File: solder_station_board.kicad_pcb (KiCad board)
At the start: 2 copper layers, 104.6 x 55.9 mm, 44 parts, among them J1 PWR_5_36, J2 Conn_FB, J3 RT_WELLER, J4 VFD dISPLAY, J5 INPUT, J6 PWR_15V, J7 INT_PWR, J8 SERIAL, J9 INPUT, P1 ISP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

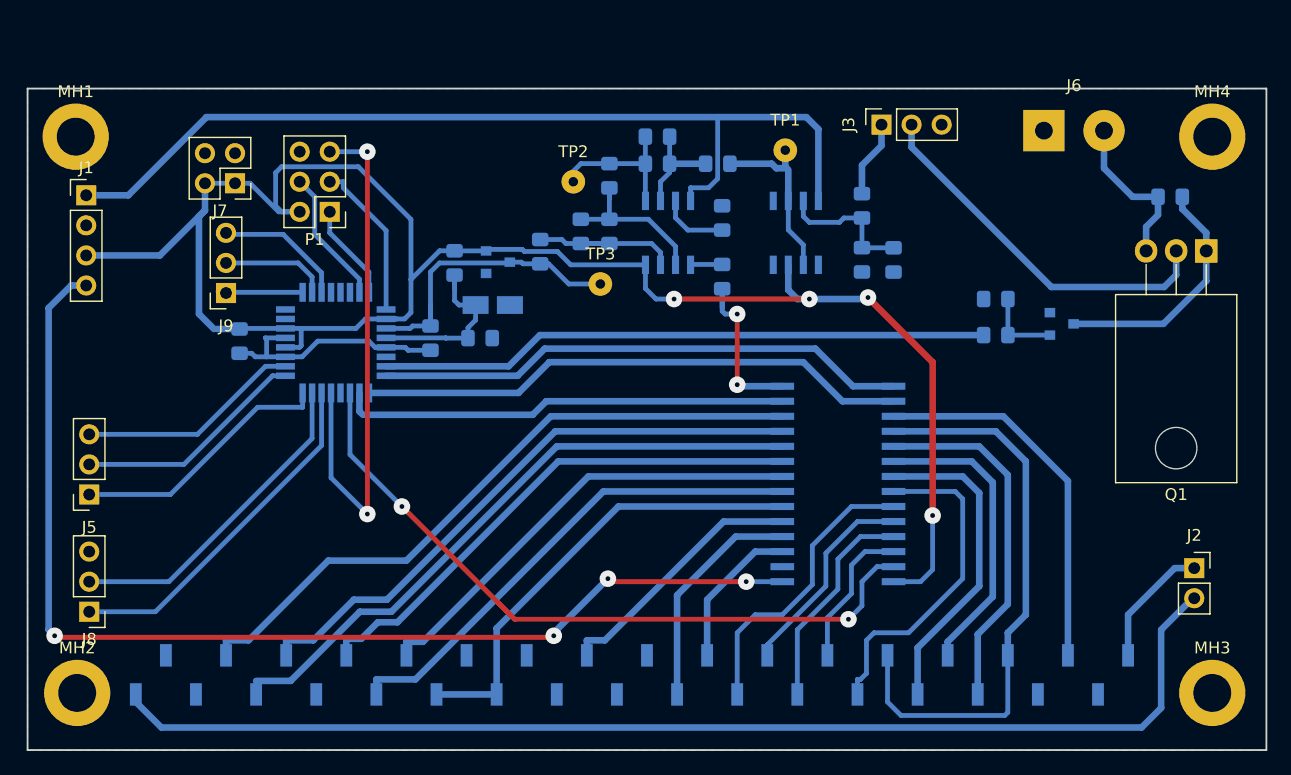
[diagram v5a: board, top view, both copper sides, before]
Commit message: new board just the adc, atmega and the pnp transistor.
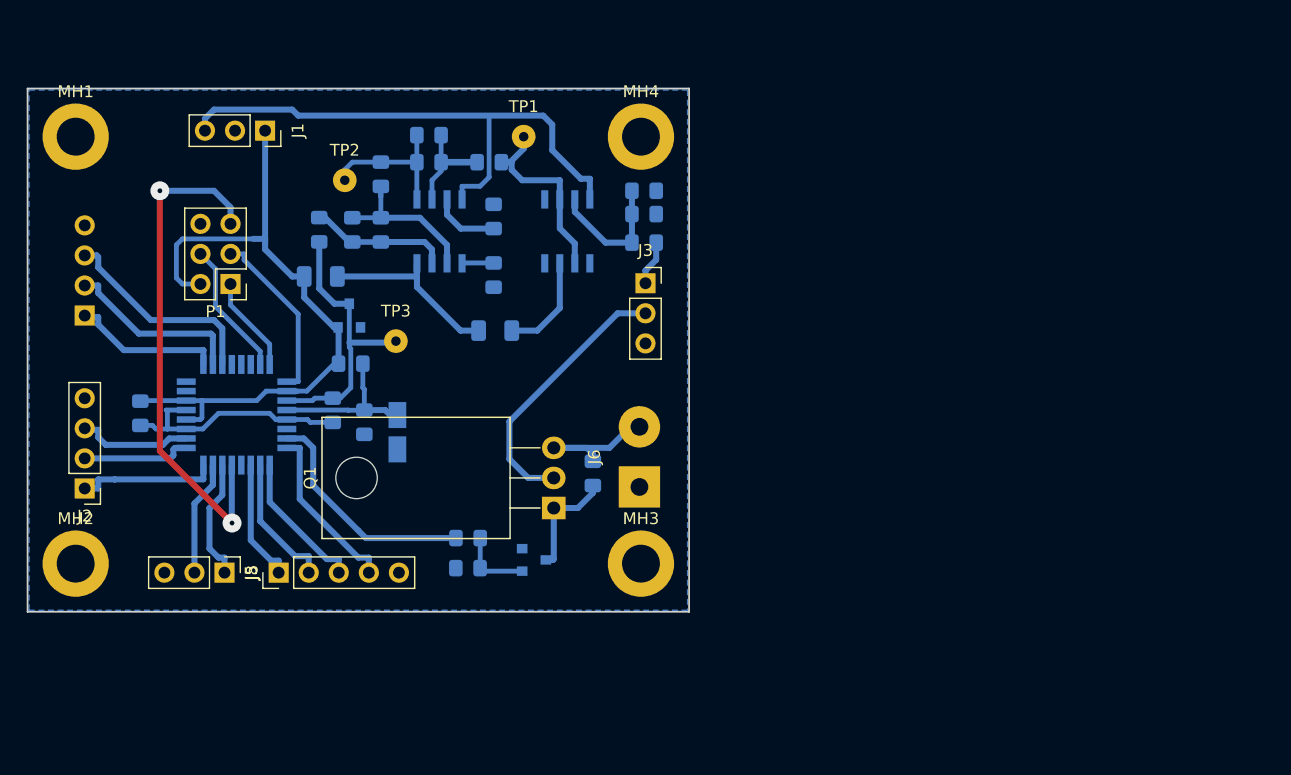
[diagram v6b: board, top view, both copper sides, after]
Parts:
- removed J7: INT_PWR, Connector_PinHeader_2.54mm:PinHeader_2x02_P2.54mm_Vertical
- removed J9: INPUT, Connector_PinSocket_2.54mm:PinSocket_1x03_P2.54mm_Vertical
- removed U7: HV5812-SOIC, Package_SO:SOIC-28W_7.5x18.7mm_P1.27mm
- added R1: 0, Resistor_SMD:R_1206_3216Metric, B.Cu at (82.4, 54.1)
- added R2: 0, Resistor_SMD:R_1206_3216Metric, B.Cu at (67.7, 49.6)
- J1: value PWR_5_36 -> PWR_5_V; footprint Connector_PinHeader_2.54mm:PinHeader_1x04_P2.54mm_Vertical -> Connector_PinSocket_2.54mm:PinSocket_1x03_P2.54mm_Vertical
- J2: value Conn_FB -> INPUT; footprint Connector_PinSocket_2.54mm:PinSocket_1x02_P2.54mm_Vertical -> Connector_PinHeader_2.54mm:PinHeader_1x04_P2.54mm_Vertical
- J4: value VFD dISPLAY -> INPUT; footprint Connector_PinSocket_2.54mm:PinSocket_1x34_P2.54mm_Vertical_SMD_Pin1Right -> Connector_PinHeader_2.54mm:PinHeader_1x04_P2.54mm_Vertical
- J5: value INPUT -> VFD_DISPLAY; footprint Connector_PinSocket_2.54mm:PinSocket_1x03_P2.54mm_Vertical -> Connector_PinHeader_2.54mm:PinHeader_1x05_P2.54mm_Vertical
- moved J2 94.0 mm to (47.7, 67.5), turned to 180 degrees
- moved Q1 59.2 mm to (87.3, 69.1), turned to 90 degrees
- moved J4 55.3 mm to (47.7, 52.9), turned to 0 degrees
- moved R6 54.1 mm to (90.6, 66.2), turned to 270 degrees
- moved R8 50.0 mm to (80.1, 74.2)
- moved MH3 49.5 mm to (94.7, 73.8)
- moved Q2 48.8 mm to (85.7, 73.5)
- moved MH4 48.3 mm to (94.7, 37.7)
- moved R9 47.8 mm to (80.1, 71.7)
- moved J6 45.5 mm to (94.6, 67.3), turned to 90 degrees
- moved J3 24.0 mm to (95.1, 50.1), turned to 0 degrees
- moved TP1 22.1 mm to (84.8, 37.7)
- moved C7 21.9 mm to (95.0, 42.3), turned to 0 degrees
- moved C1 19.3 mm to (76.8, 37.6)
- moved C2 19.3 mm to (70.3, 45.6)
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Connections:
- J1 pad 1: -5V -> +5V
- J1 pad 3: +5V -> -5V
- J2 pad 1: /FBB -> /INP1
- J2 pad 2: /FBA -> /INP2
- J4 pad 1: /FBA -> /INP4
- J4 pad 2: (no net) -> /INP5
- J4 pad 3: (no net) -> /INP6
- J4 pad 4: /S8 -> GND
- J5 pad 1: /INP1 -> /VFD_DATA
- J5 pad 2: /INP2 -> /VFD_RCLK
- J5 pad 3: /INP3 -> /VFD_SRCLK
- U6 pad 24: /CLOCK -> /VFD_SRCLR
- U6 pad 25: /STROBE -> /VFD_SRCLK
- U6 pad 26: /BLANK -> /VFD_RCLK
- U6 pad 27: /SDI -> /VFD_DATA
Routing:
- net /FBA: track 99.3 -> 0.00 mm
- net +36V: track 95.7 -> 0.00 mm, vias 4 -> 0
- net +5V: track 161.5 -> 85.1 mm, vias 4 -> 0
- net /SOLDER: track 88.6 -> 19.6 mm
- net /6G: track 63.2 -> 0.00 mm
- net /SDI: track 61.5 -> 0.00 mm, vias 2 -> 0
- net /S5: track 57.4 -> 0.00 mm
- net /S8: track 56.1 -> 0.00 mm
- net /7G: track 53.8 -> 0.00 mm
- net /S7: track 50.5 -> 0.00 mm
- net /1G: track 48.7 -> 0.00 mm
- net /STROBE: track 46.8 -> 0.00 mm
- net /CLOCK: track 45.1 -> 0.00 mm
- net /5G: track 39.1 -> 0.00 mm
- net /S4: track 38.7 -> 0.00 mm
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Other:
- board size 104.6 x 55.9 mm -> 55.9 x 44.2 mm

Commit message: remove 0R resistors
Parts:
- removed R1, R2: 0, Resistor_SMD:R_1206_3216Metric
- MH1, MH2, MH3, MH4: value MountingHole_Pad -> MP
- moved R10 2.45 mm to (82.8, 37.6)
- moved TP1 1.65 mm to (86.4, 37.7)
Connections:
- net /VFD_SRCLR renamed /~VFD_SRCLR
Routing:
- net +5V: track 85.1 -> 99.9 mm, vias 0 -> 3
- net /MOSI: track 11.4 -> 15.5 mm
- net Net-(C1-Pad1): track 8.79 -> 11.1 mm
- net Net-(R10-Pad1): track 16.9 -> 15.4 mm
- net /SCK: track 14.8 -> 15.9 mm
- net Net-(C7-Pad1): track 11.3 -> 11.9 mm
- net -5V: track 48.1 -> 48.5 mm, vias 0 -> 2
- added copper zone on F.Cu, net GND

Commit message: small arrangements
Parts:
- removed C13, C8, C9: 10n, Capacitor_SMD:C_0805_2012Metric_Pad1.15x1.40mm_HandSolder
- removed D8: 4V7, Diode_SMD:D_MicroMELF_Hadsoldering
- removed J8: SERIAL, Connector_PinHeader_2.54mm:PinHeader_1x03_P2.54mm_Vertical
- removed R13, R16: 1k, Resistor_SMD:R_0805_2012Metric_Pad1.15x1.40mm_HandSolder
- removed R14: 33k, Resistor_SMD:R_0805_2012Metric_Pad1.15x1.40mm_HandSolder
- removed R15: 10K, Resistor_SMD:R_0805_2012Metric_Pad1.15x1.40mm_HandSolder
- removed TP2, TP3: tp, Connector_Wire:SolderWirePad_1x01_Drill0.8mm
- removed U4: TLC272, Package_SO:SOIC-8_3.9x4.9mm_P1.27mm
- removed U5: LT1007, Package_SO:SOIC-8_3.9x4.9mm_P1.27mm
- removed U6: ATMEGA168-20AU, Package_QFP:TQFP-32_7x7mm_P0.8mm
- added C3: 10n, Capacitor_SMD:C_0805_2012Metric_Pad1.15x1.40mm_HandSolder, F.Cu at (53.8, 50.7)
- added C4: 10n, Capacitor_SMD:C_0805_2012Metric_Pad1.15x1.40mm_HandSolder, F.Cu at (78.4, 53.2)
- added C5: 100n, Capacitor_SMD:C_0805_2012Metric_Pad1.15x1.40mm_HandSolder, F.Cu at (56.5, 65.4)
- added C6: 100u, Capacitor_THT:C_Radial_D8.0mm_H7.0mm_P3.50mm, F.Cu at (71.0, 73.4)
- added D2: 4V7, Diode_SMD:D_MicroMELF_Hadsoldering, F.Cu at (75.1, 46.6)
- added D3: LED_G, LED_THT:LED_D3.0mm, F.Cu at (83.8, 37.0)
- added J7: INPUT, Connector_PinHeader_2.54mm:PinHeader_1x04_P2.54mm_Vertical, F.Cu at (50.0, 59.6)
- added L1: 10u, Inductor_SMD:L_1206_3216Metric_Pad1.42x1.75mm_HandSolder, F.Cu at (64.6, 70.8)
- added R1: 10M, Resistor_SMD:R_0805_2012Metric_Pad1.15x1.40mm_HandSolder, F.Cu at (92.0, 43.7)
- added R2: 5k6, Resistor_SMD:R_0805_2012Metric_Pad1.15x1.40mm_HandSolder, F.Cu at (92.0, 46.0)
- added R3: 100k, Resistor_SMD:R_0805_2012Metric_Pad1.15x1.40mm_HandSolder, F.Cu at (87.5, 46.0)
- added U1: OPA343, Package_TO_SOT_SMD:SOT-23-5, F.Cu at (81.9, 47.9)
- added U2: ATMEGA168-20AU, Package_QFP:TQFP-32_7x7mm_P0.8mm, F.Cu at (61.4, 49.7)
- C1, C2, D1, Q2, R11, R4: moved to F.Cu
- C7: value 10n -> 100n; moved to F.Cu
- J1: value PWR_5_V -> RT_WELLER
- J2: value INPUT -> SERIAL; footprint Connector_PinHeader_2.54mm:PinHeader_1x04_P2.54mm_Vertical -> Connector_PinHeader_2.54mm:PinHeader_1x03_P2.54mm_Vertical
- J3: value RT_WELLER -> PWR_15V; footprint Connector_PinSocket_2.54mm:PinSocket_1x03_P2.54mm_Vertical -> Connector_Wire:SolderWirePad_1x02_P5.08mm_Drill1.5mm
- J4: value INPUT -> PWR_5V; footprint Connector_PinHeader_2.54mm:PinHeader_1x04_P2.54mm_Vertical -> Connector_PinHeader_2.54mm:PinHeader_1x02_P2.54mm_Vertical; moved to F.Cu
- J6: value PWR_15V -> ENCODER; footprint Connector_Wire:SolderWirePad_1x02_P5.08mm_Drill1.5mm -> Connector_PinHeader_2.54mm:PinHeader_1x05_P2.54mm_Vertical
- MH1, MH2, MH3, MH4: value MP -> MH_Pad
- R10: value 1k -> 4k7; moved to F.Cu
- R12: value 22k -> 648; moved to F.Cu
- R5: value 5k6 -> 68k; moved to F.Cu
- R6: value 4k7 -> 100; moved to F.Cu
- R7: value 100k -> 5k6; moved to F.Cu
- R8: value 2k2 -> 1k; moved to F.Cu
- R9: value 1k -> 2k2; moved to F.Cu
- TP1: value tp -> TEMP; footprint Connector_Wire:SolderWirePad_1x01_Drill0.8mm -> TestPoint:TestPoint_Loop_D2.60mm_Drill0.9mm_Beaded
- moved MH3 58.4 mm to (49.2, 37.2)
- moved J6 50.3 mm to (49.9, 44.3), turned to 0 degrees
- moved MH2 44.7 mm to (91.7, 74.3)
- moved C7 40.7 mm to (61.3, 65.2), turned to 270 degrees
- moved J5 38.8 mm to (69.8, 36.2)
- moved MH1 36.6 mm to (49.2, 74.3)
- moved J2 34.2 mm to (61.7, 36.2), turned to 270 degrees
- moved J1 33.9 mm to (92.3, 54.1), turned to 0 degrees
- moved R10 31.4 mm to (90.6, 68.0), turned to 0 degrees
- moved J4 28.3 mm to (66.4, 74.1), turned to 270 degrees
- moved R8 26.6 mm to (88.0, 48.8)
- moved J3 25.9 mm to (85.2, 74.1), turned to 180 degrees
- moved R6 24.2 mm to (82.0, 43.6), turned to 0 degrees
- moved R9 22.0 mm to (88.0, 51.1)
- moved TP1 21.9 mm to (70.1, 52.2)
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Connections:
- C1 pad 2: Net-(C1-Pad2) -> GND
- C2 pad 2: Net-(C2-Pad2) -> GND
- J1 pad 1: +5V -> Net-(J1-Pad1)
- J1 pad 2: GND -> Net-(J1-Pad2)
- J1 pad 3: -5V -> GND
- J2 pad 1: /INP1 -> /RX
- J2 pad 2: /INP2 -> /TX
- J2 pad 3: /INP3 -> GND
- J3 pad 1: Net-(J3-Pad1) -> GND
- J3 pad 2: Net-(J3-Pad2) -> +15V
- J4 pad 1: /INP4 -> GND
- J4 pad 2: /INP5 -> +5V
- J6 pad 1: GND -> /INP1
- J6 pad 2: +15V -> /INP2
- Q1 pad 2: Net-(J3-Pad2) -> Net-(J1-Pad2)
- R10 pad 1: Net-(R10-Pad1) -> +15V
- R10 pad 2: Net-(C1-Pad1) -> Net-(Q1-Pad1)
- R11 pad 2: Net-(C8-Pad1) -> /RST
- R12 pad 1: Net-(C1-Pad1) -> Net-(D3-Pad2)
- R12 pad 2: Net-(C1-Pad2) -> +5V
- R4 pad 1: Net-(R4-Pad1) -> +5V
- R4 pad 2: GND -> Net-(C2-Pad1)
- R5 pad 1: Net-(C7-Pad1) -> Net-(R5-Pad1)
- R5 pad 2: Net-(J3-Pad1) -> Net-(R5-Pad2)
- R6 pad 1: +15V -> Net-(R5-Pad2)
- R6 pad 2: Net-(Q1-Pad1) -> GND
- R7 pad 1: GND -> /TEMP
- R7 pad 2: Net-(C7-Pad1) -> Net-(R5-Pad1)
- R8 pad 1: GND -> /SOLDER
- R9 pad 1: /SOLDER -> GND
- TP1 pad 1: Net-(R10-Pad1) -> /TEMP
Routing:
- net -5V: track 48.5 -> 0.00 mm, vias 2 -> 0
- net +5V: track 99.9 -> 130.0 mm
- net Net-(J3-Pad2): track 22.9 -> 0.00 mm
- net GND: track 20.5 -> 42.0 mm
- net Net-(C7-Pad1): track 11.9 -> 28.0 mm
- net Net-(R10-Pad1): track 15.4 -> 0.00 mm
- net +15V: track 12.1 -> 26.4 mm
- net Net-(C2-Pad2): track 14.2 -> 0.00 mm
- net /MISO: track 8.39 -> 22.3 mm, vias 0 -> 1
- net Net-(C8-Pad1): track 13.9 -> 0.00 mm
- net /MOSI: track 15.5 -> 28.3 mm
- net Net-(C1-Pad2): track 12.7 -> 0.00 mm
- net /RST: track 43.4 -> 56.0 mm
- net Net-(J1-Pad2): track 0.00 -> 12.3 mm
- net Net-(J8-Pad2): track 11.2 -> 0.00 mm
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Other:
- board size 55.9 x 44.2 mm -> 49.5 x 44.2 mm
- net class power added: clearance 0.2, trace_width 0.4064, via_dia 0.8, via_drill 0.4
- board text added: "+"
- board text added: "-"
- board text added: "A"
- board text added: "B"
- board text added: "ENCODER"
- board text added: "ISP"
- board text added: "PWR_12V"
- board text added: "PWR_5V"
- board text added: "RT_WELLER"
- board text added: "SERIAL"
- board text added: "VFD_DISPLAY"
